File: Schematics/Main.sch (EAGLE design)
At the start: 15 parts, among them U1 LCD-16X2SILK, X1 USBPTH

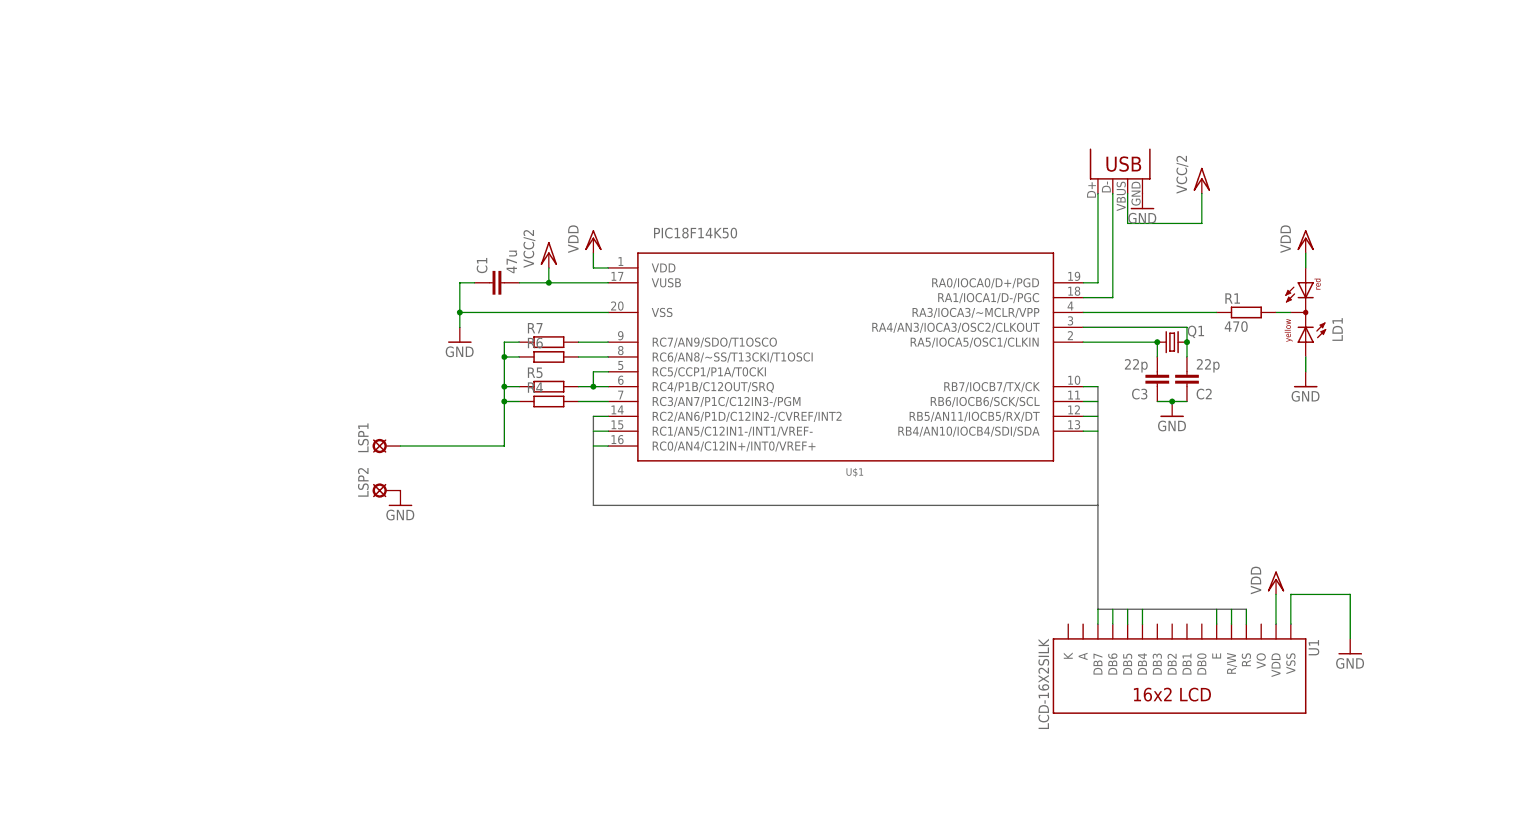
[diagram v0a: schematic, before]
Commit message: Schematic complete
Board nearly complete, only one route missing. Will see if 2 resistors are enough to condition the signal.

Signed-off-by: Aljaž Srebrnič <a2piratesoft@gmail.com>
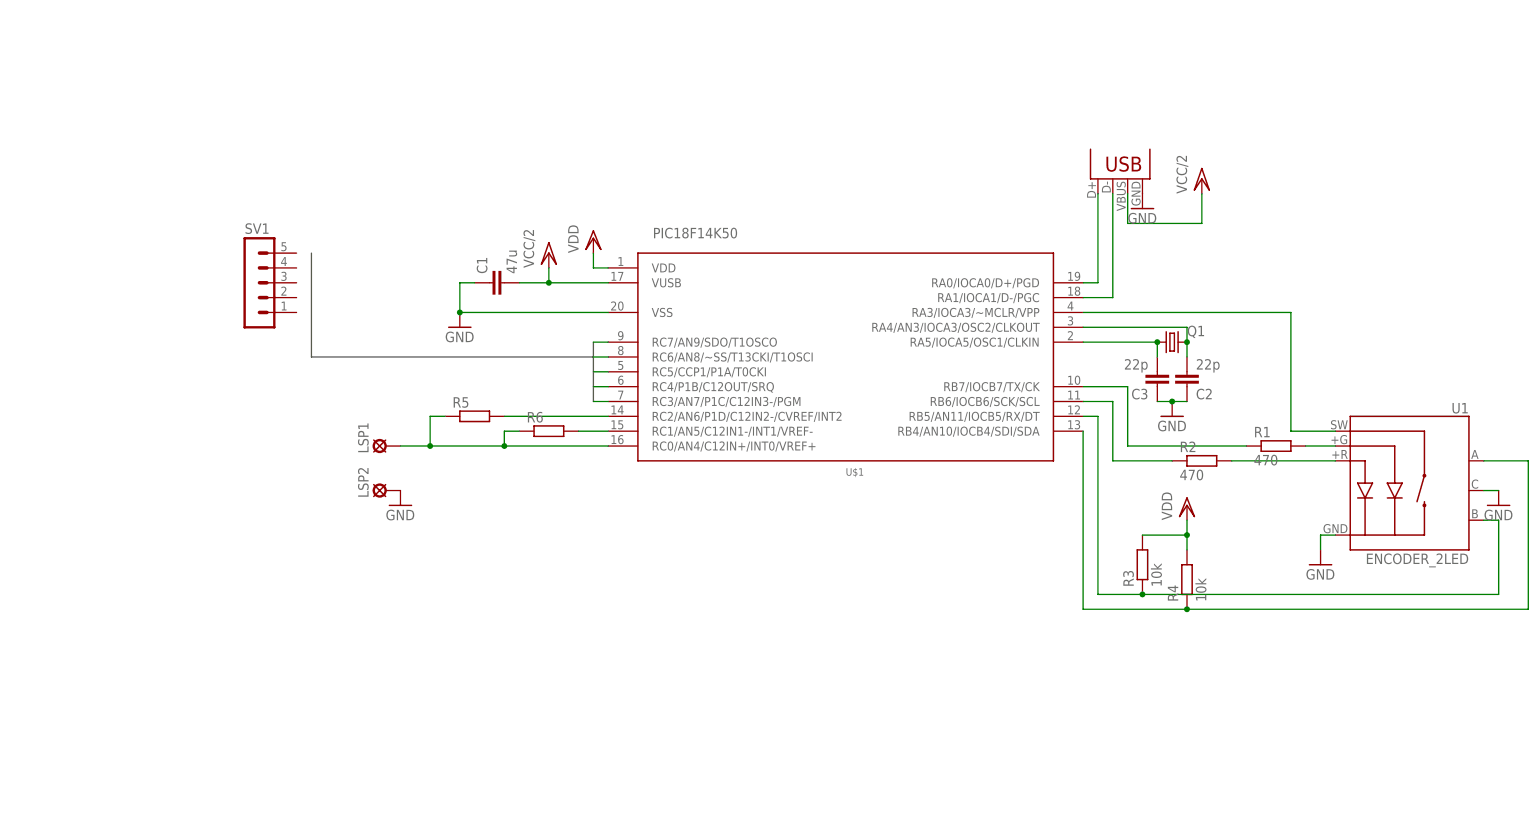
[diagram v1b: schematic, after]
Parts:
- removed LD1: (no value), led:DUOLED-RY-C
- removed R7: (no value), rcl:R-EU_0204/7
- added R2: 470, rcl:R-EU_0207/7
- added R3: 10k, rcl:R-EU_0207/7
- added SV1: (no value), con-lstb:MA05-1
- R1, R5, R6: device rcl:R-EU_0204/7 -> rcl:R-EU_0207/7
- R4: value (none) -> 10k; device rcl:R-EU_0204/7 -> rcl:R-EU_0207/7
- U1: value LCD-16X2SILK -> ENCODER_2LED; device SparkFun:LCD-16X2SILK -> SparkFun:ENCODER_2LED
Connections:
- removed net DB4: U$1.RB4/AN10/IOCB4/SDI/SDA, U1.DB4
- removed net DB5: U$1.RB5/AN11/IOCB5/RX/DT, U1.DB5
- removed net DB6: U$1.RB6/IOCB6/SCK/SCL, U1.DB6
- removed net DB7: U$1.RB7/IOCB7/TX/CK, U1.DB7
- removed net E: U$1.RC2/AN6/P1D/C12IN2-/CVREF/INT2, U1.E
- removed net R/W: U$1.RC1/AN5/C12IN1-/INT1/VREF-, U1.R/W
- removed net RS: U$1.RC0/AN4/C12IN+/INT0/VREF+, U1.RS
- new net D/~C: U$1.RC5/CCP1/P1A/T0CKI
- new net N$10: R2.1, U$1.RB6/IOCB6/SCK/SCL
- new net N$11: R3.1, U$1.RB5/AN11/IOCB5/RX/DT, U1.B
- new net N$14: R5.2, U$1.RC2/AN6/P1D/C12IN2-/CVREF/INT2
- new net SCLK: U$1.RC6/AN8/~SS/T13CKI/T1OSCI
- new net SDIN: U$1.RC7/AN9/SDO/T1OSCO
- new net ~RES: U$1.RC3/AN7/P1C/C12IN3-/PGM
- new net ~SCE: U$1.RC4/P1B/C12OUT/SRQ
- net GND: now also U1.-, U1.C; no longer LD1.AY, U1.VSS
- net N$12: now also U$1.RB4/AN10/IOCB4/SDI/SDA, U1.A; no longer LSP1.MP, R5.1, R6.1, R7.1
- net N$13: now also R6.2, U$1.RC1/AN5/C12IN1-/INT1/VREF-; no longer R1.1, U$1.RA3/IOCA3/~MCLR/VPP
- net N$5: now also U$1.RA3/IOCA3/~MCLR/VPP, U1.SW; no longer R7.2, U$1.RC7/AN9/SDO/T1OSCO
- net N$6: now also R1.1, U$1.RB7/IOCB7/TX/CK; no longer R6.2, U$1.RC6/AN8/~SS/T13CKI/T1OSCI
- net N$7: now also R1.2, U1.+G; no longer R5.2, U$1.RC4/P1B/C12OUT/SRQ, U$1.RC5/CCP1/P1A/T0CKI
- net N$8: now also LSP1.MP, R5.1, R6.1, U$1.RC0/AN4/C12IN+/INT0/VREF+; no longer R4.2, U$1.RC3/AN7/P1C/C12IN3-/PGM
- net N$9: now also R2.2, U1.+R; no longer LD1.C, R1.2
- net VDD: now also R3.2, R4.2; no longer LD1.AR, U1.VDD
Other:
- moved on the sheet: R1, R4, R5, R6

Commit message: Schematics competed
Updated to use rotary encoder and nokia graphic screen.

Signed-off-by: Aljaž Srebrnič <a2piratesoft@gmail.com>
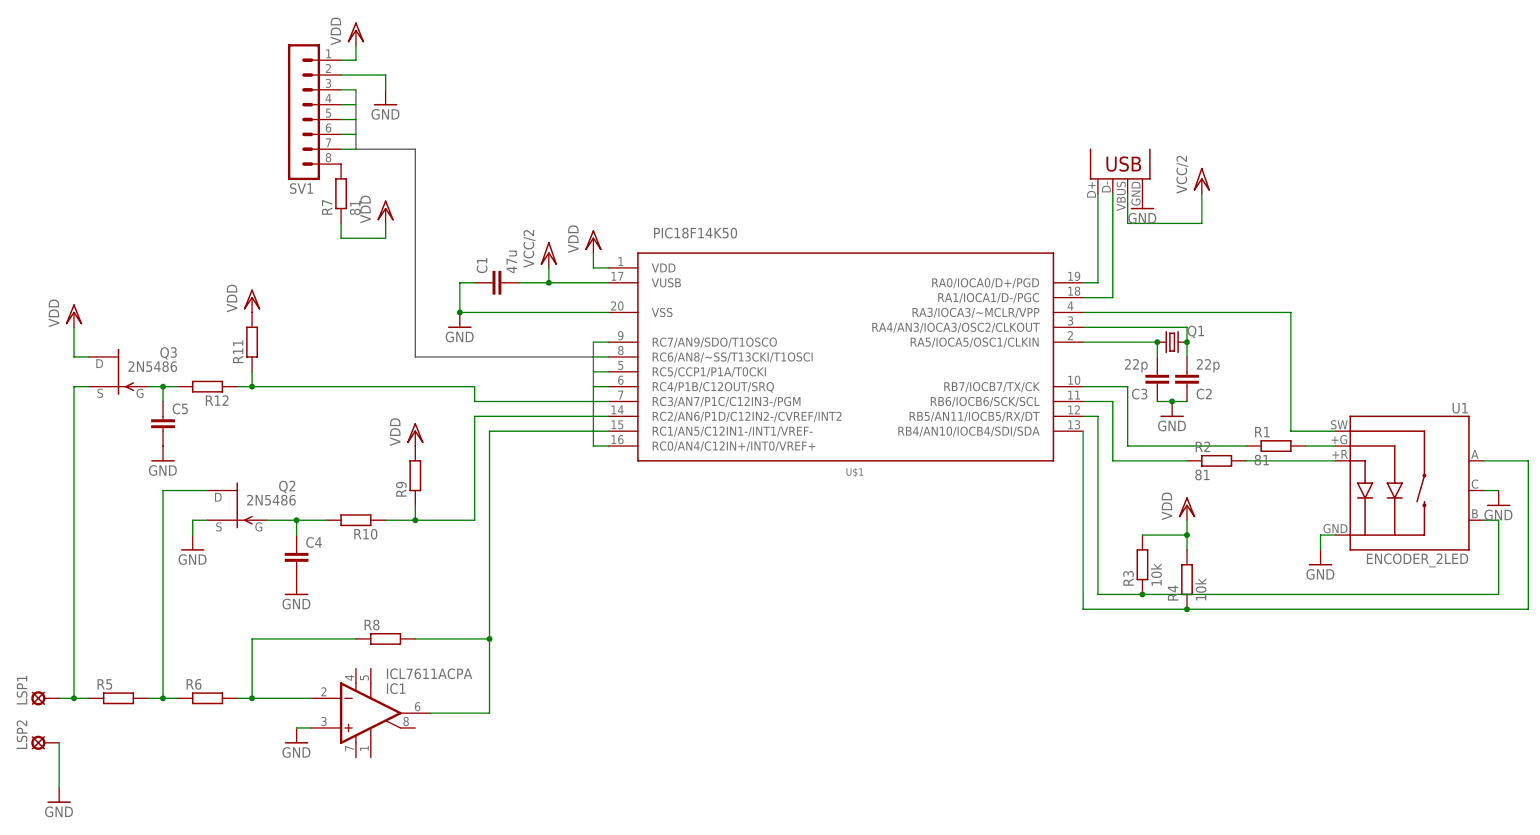
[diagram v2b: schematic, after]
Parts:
- added C4, C5: (no value), rcl:C-EU025-025X050
- added IC1: ICL7611ACPA, maxim:ICL7611ACPA
- added Q2, Q3: 2N5486, transistor-fet:2N5486
- added R10, R11, R12, R8, R9: (no value), rcl:R-EU_0207/7
- added R7: 81, rcl:R-EU_0207/7
- R1, R2: value 470 -> 81
- SV1: device con-lstb:MA05-1 -> con-lstb:MA08-1
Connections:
- new net N$15: R7.2, SV1.8
- new net N$16: IC1.OUT, R8.2, U$1.RC1/AN5/C12IN1-/INT1/VREF-
- new net N$17: R10.1, R9.1, U$1.RC2/AN6/P1D/C12IN2-/CVREF/INT2
- new net N$18: R11.1, R12.1, U$1.RC3/AN7/P1C/C12IN3-/PGM
- new net N$19: C4.1, Q2.G, R10.2
- new net N$20: C5.1, Q3.G, R12.2
- net D/~C: now also SV1.5
- net GND: now also C4.2, C5.2, IC1.+IN, Q2.S, SV1.2
- net N$13: now also IC1.-IN, R8.1; no longer U$1.RC1/AN5/C12IN1-/INT1/VREF-
- net N$14: now also LSP1.MP, Q3.S, R5.1; no longer R5.2, U$1.RC2/AN6/P1D/C12IN2-/CVREF/INT2
- net N$8: now also Q2.D, R5.2; no longer LSP1.MP, R5.1, U$1.RC0/AN4/C12IN+/INT0/VREF+
- net SCLK: now also SV1.7
- net SDIN: now also SV1.6
- net VDD: now also Q3.D, R11.2, R7.1, R9.2, SV1.1
- net ~RES: now also SV1.4, U$1.RC0/AN4/C12IN+/INT0/VREF+; no longer U$1.RC3/AN7/P1C/C12IN3-/PGM
- net ~SCE: now also SV1.3
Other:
- moved on the sheet: LSP1, LSP2, R2, R5, R6

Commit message: Using VGA and VCR
Using variable gain amplifier for input and a VCR to inject signals

Signed-off-by: Aljaž "g5pw" Srebrnič <a2piratesoft@gmail.com>
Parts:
- removed R11, R9: (no value), rcl:R-EU_0207/7
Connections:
- new net N$21: Q3.S, R6.1
- net GND: now also R5.1; no longer IC1.+IN, Q2.S
- net N$13: now also Q2.S, R5.2; no longer R6.2, R8.1
- net N$14: now also IC1.+IN, R6.2; no longer Q3.S, R5.1
- net N$17: no longer R9.1
- net N$18: no longer R11.1
- net N$8: now also R8.1; no longer R5.2, R6.1
- net VDD: no longer R11.2, R9.2
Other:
- moved on the sheet: C4, IC1, LSP1, LSP2, Q2, R10, R5, R6, R8
